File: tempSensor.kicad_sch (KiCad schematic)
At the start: 4 parts, among them U2 TMP175AIDR

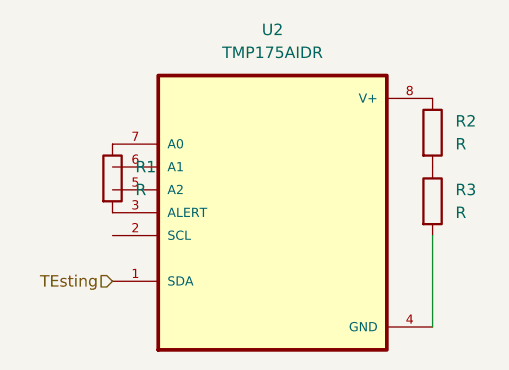
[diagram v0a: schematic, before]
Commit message: Added pins to temp sensor
Hierarchy input/output for the sensor schematic and the root
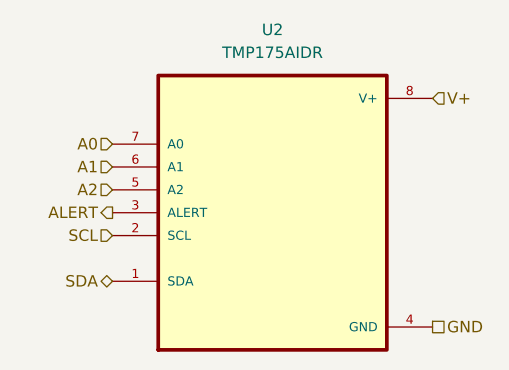
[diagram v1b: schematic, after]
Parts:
- removed R1, R2, R3: R, symbol Device:R
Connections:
- net SCL: now reaches U2.2 (SCL)
- net ALERT: now reaches U2.3 (ALERT)
- net GND: now reaches U2.4 (GND)
- net A2: now reaches U2.5 (A2)
- net A1: now reaches U2.6 (A1)
- net A0: now reaches U2.7 (A0)
- net V+: now reaches U2.8 (V+)
- net TEsting renamed SDA

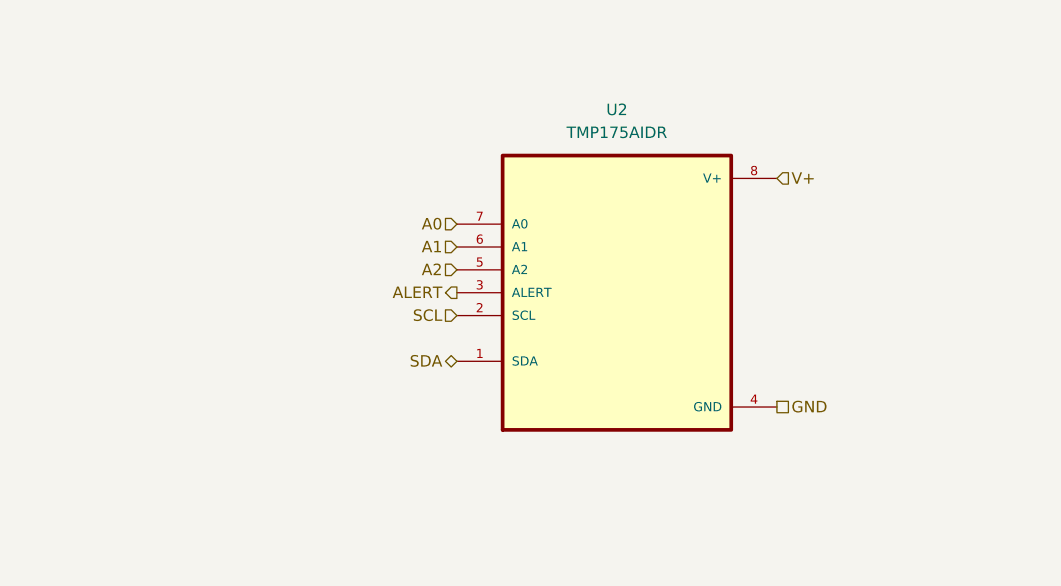
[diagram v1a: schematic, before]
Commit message: Added layout components and comment
Bypass capacitor and pullup resistors according to datasheet
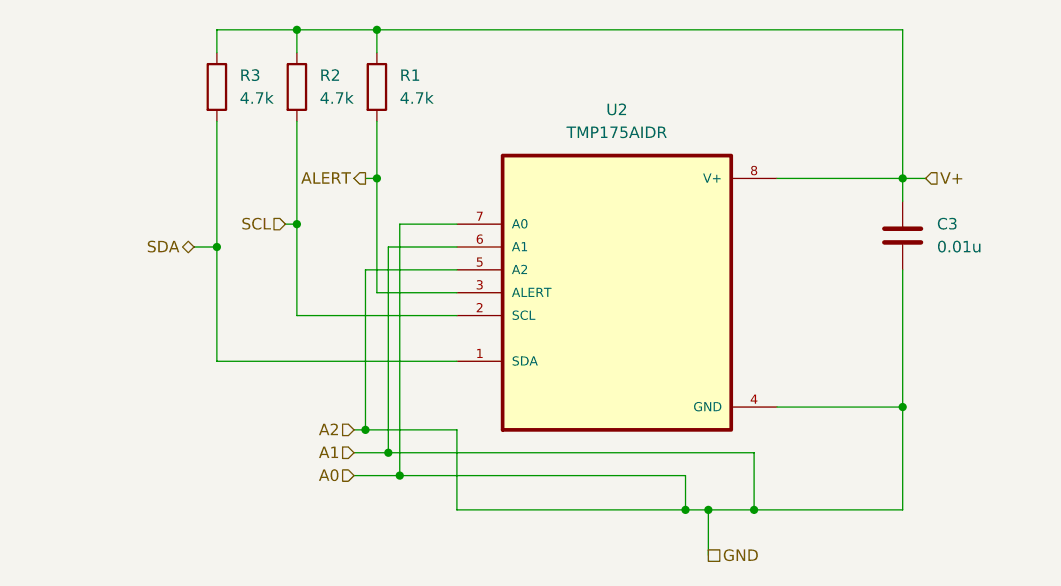
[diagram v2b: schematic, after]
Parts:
- added C3: 0.01u, symbol Device:C
- added R1, R2, R3: 4.7k, symbol Device:R
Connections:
- net A1 is gone; now on net A0: U2.6 (A1)
- net A2 is gone; now on net A0: U2.5 (A2)
- net GND is gone; now on net A0: U2.4 (GND)
- net A0: now also C3.2
- net ALERT: now also R1.2
- net SCL: now also R2.2
- net SDA: now also R3.2
- net V+: now also C3.1, R1.1, R2.1, R3.1

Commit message: Cleanup temperature sensor
Reconnected grounds and removed useless pins
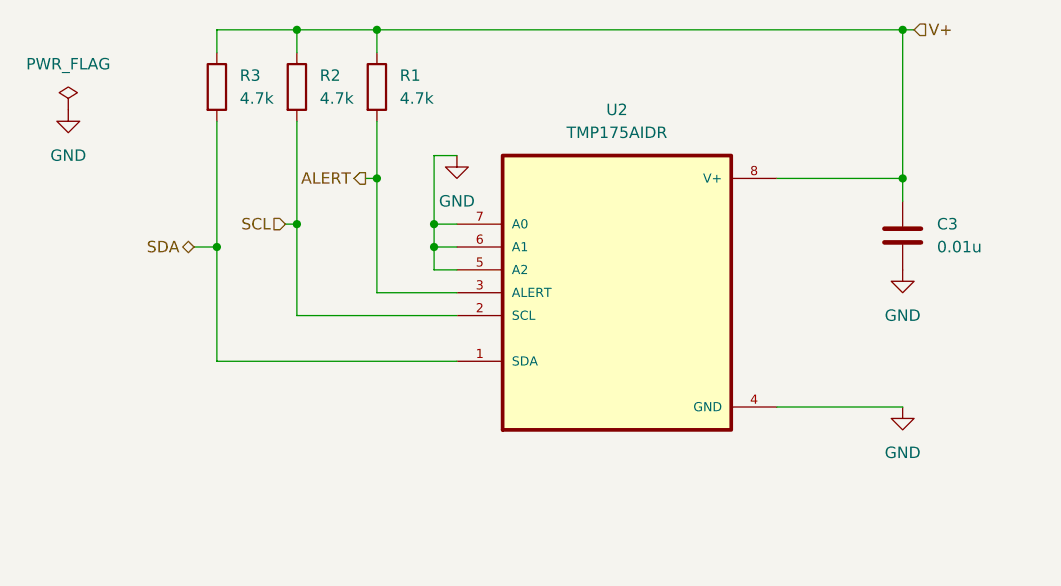
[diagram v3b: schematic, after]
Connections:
- net A0 renamed GND

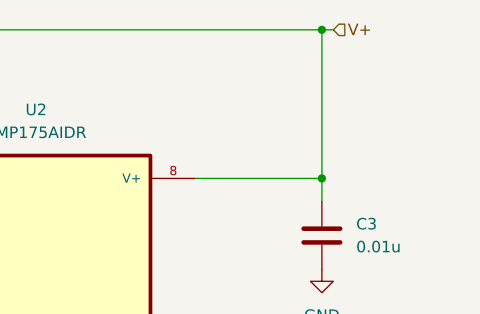
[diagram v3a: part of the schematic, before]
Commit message: Added microprocessor connections
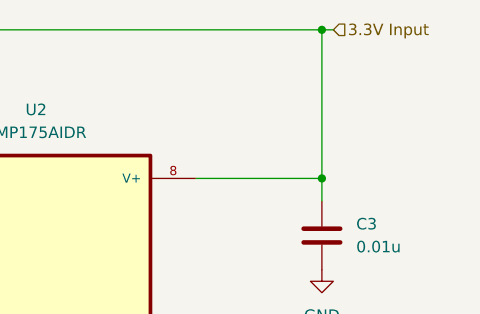
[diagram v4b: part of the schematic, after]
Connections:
- net V+ renamed 3.3V Input
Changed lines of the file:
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@@
 		)
 	)
-	(hierarchical_label "V+"
+	(hierarchical_label "3.3V Input"
 		(shape input)
 		(at 171.45 54.61 0)
@@
 		)
 		(instances
-			(project ""
+			(project "plant caretaker"
 				(path "/23b35dcc-615e-4aec-abee-c26cc3d8b906/f322dacc-209e-46f8-9f8f-6103b236b6bb"
 					(reference "C3")
@@
 		)
 		(instances
-			(project ""
+			(project "plant caretaker"
 				(path "/23b35dcc-615e-4aec-abee-c26cc3d8b906/f322dacc-209e-46f8-9f8f-6103b236b6bb"
 					(reference "#PWR029")
@@
 		)
 		(instances
-			(project ""
+			(project "plant caretaker"
 				(path "/23b35dcc-615e-4aec-abee-c26cc3d8b906/f322dacc-209e-46f8-9f8f-6103b236b6bb"
 					(reference "R1")
@@
 		)
 		(instances
-			(project ""
+			(project "plant caretaker"
 				(path "/23b35dcc-615e-4aec-abee-c26cc3d8b906/f322dacc-209e-46f8-9f8f-6103b236b6bb"
 					(reference "#FLG05")

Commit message: Cleanup, sorting, adding external parts
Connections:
- net 3.3V Input renamed 3.3V_IN
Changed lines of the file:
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@@
 		)
 	)
-	(hierarchical_label "3.3V Input"
+	(hierarchical_label "3.3V_IN"
 		(shape input)
 		(at 171.45 54.61 0)

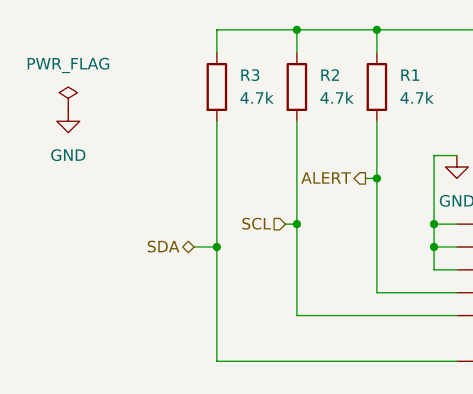
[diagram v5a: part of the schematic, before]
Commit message: Added Kitronik and cleaned connections
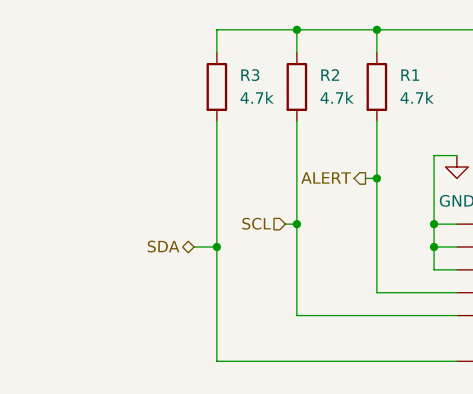
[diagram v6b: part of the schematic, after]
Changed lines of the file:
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@@
-	)
-	(symbol
-		(lib_id "power:GND")
-		(at 77.47 63.5 0)
-		(unit 1)
-		(exclude_from_sim no)
-		(in_bom yes)
-		(on_board yes)
-		(dnp no)
-		(fields_autoplaced yes)
-		(property "Reference" "#PWR030"
-			(at 77.47 69.85 0)
-			(effects
-				(font
-					(size 1.27 1.27)
-				)
-				(hide yes)
-			)
-		)
-		(property "Value" "GND"
-			(at 77.47 68.58 0)
-			(effects
-				(font
-					(size 1.27 1.27)
-				)
-			)
-		)
-		(property "Footprint" ""
-			(at 77.47 63.5 0)
-			(effects
-				(font
-					(size 1.27 1.27)
-				)
-				(hide yes)
-			)
-		)
-		(property "Datasheet" ""
-			(at 77.47 63.5 0)
-			(effects
-				(font
-					(size 1.27 1.27)
-				)
-				(hide yes)
-			)
-		)
-		(property "Description" "Power symbol creates a global label with name \"GND\" , ground"
-			(at 77.47 63.5 0)
-			(effects
-				(font
-					(size 1.27 1.27)
-				)
-				(hide yes)
-			)
-		)
-		(pin "1"
-		)
-		(instances
-			(project "plant caretaker"
-				(path "/23b35dcc-615e-4aec-abee-c26cc3d8b906/f322dacc-209e-46f8-9f8f-6103b236b6bb"
-					(reference "#PWR030")
-					(unit 1)
-				)
-			)
-		)
 	)
 	(symbol
@@
 					(unit 1)
 				)
-			)
-		)
-	)
-	(symbol
-		(lib_id "power:PWR_FLAG")
-		(at 77.47 63.5 0)
-		(unit 1)
-		(exclude_from_sim no)
-		(in_bom yes)
-		(on_board yes)
-		(dnp no)
-		(fields_autoplaced yes)
-		(property "Reference" "#FLG05"
-			(at 77.47 61.595 0)
-			(effects
-				(font
-					(size 1.27 1.27)
-				)
-				(hide yes)
-			)
-		)
-		(property "Value" "PWR_FLAG"
-			(at 77.47 58.42 0)
-			(effects
-				(font
-					(size 1.27 1.27)
-				)
-			)
-		)
-		(property "Footprint" ""
-			(at 77.47 63.5 0)
-			(effects
-				(font
-					(size 1.27 1.27)
-				)
-				(hide yes)
-			)
-		)
-		(property "Datasheet" "~"
-			(at 77.47 63.5 0)
-			(effects
-				(font
-					(size 1.27 1.27)
-				)
-				(hide yes)
-			)
-		)
-		(property "Description" "Special symbol for telling ERC where power comes from"
-			(at 77.47 63.5 0)
-			(effects
-				(font
-					(size 1.27 1.27)
-				)
-				(hide yes)
-			)
-		)
-		(pin "1"
-		)
-		(instances
-			(project "plant caretaker"
-				(path "/23b35dcc-615e-4aec-abee-c26cc3d8b906/f322dacc-209e-46f8-9f8f-6103b236b6bb"
-					(reference "#FLG05")
-					(unit 1)
-				)

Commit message: Added basic footprint to ESP32
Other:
- title: (none) -> Temperature sensor
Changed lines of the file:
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@@
 	(generator_version "8.0")
 	(paper "A4")
+	(title_block
+		(title "Temperature sensor")
+		(date "2024-12-12")
+	)
 	(junction
 		(at 170.18 54.61)

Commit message: Added footprints and imported to PCB
All of them except speakers
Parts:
- C3: footprint (none) -> Capacitor_SMD:C_0603_1608Metric
- R1, R2, R3: footprint (none) -> Resistor_SMD:R_0603_1608Metric
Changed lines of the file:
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@@
 			)
 		)
-		(property "Footprint" ""
+		(property "Footprint" "Resistor_SMD:R_0603_1608Metric"
 			(at 92.202 60.96 90)
 			(effects
@@
 			)
 		)
-		(property "Footprint" ""
+		(property "Footprint" "Resistor_SMD:R_0603_1608Metric"
 			(at 101.092 60.96 90)
 			(effects
@@
 			)
 		)
-		(property "Footprint" ""
+		(property "Footprint" "Capacitor_SMD:C_0603_1608Metric"
 			(at 171.1452 81.28 0)
 			(effects
@@
 			)
 		)
-		(property "Footprint" ""
+		(property "Footprint" "Resistor_SMD:R_0603_1608Metric"
 			(at 109.982 60.96 90)
 			(effects
